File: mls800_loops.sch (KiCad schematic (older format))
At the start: 52 parts, among them J10 JACK_2P_STACK, J11 JACK_2P_SW, J2 JACK_2P_SW, J3 JACK_2P_STACK, J4 JACK_2P_STACK, J5 JACK_2P_STACK, J6 JACK_2P_STACK, J7 JACK_2P_STACK, J8 JACK_2P_STACK, J9 JACK_2P_STACK, Q1 2N3904, Q10 2N3904, Q11 2N3904, Q12 2N3904, Q13 2N3904, Q14 2N3904, Q15 2N3904, Q16 2N3904, Q2 2N3904, Q3 2N3904, Q4 2N3904, Q5 2N3904, Q6 2N3904, Q7 2N3904, Q8 2N3904, Q9 2N3904, U4 MCP23017

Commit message: MLS800
* unsplit AGND and DGND
* retouted relays
* relayout of gnd zone
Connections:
- net labels added: GND
- net labels removed: DGND
- wire segments 286 -> 289

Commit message: MLS800
* changed AGND to GND in jack connectors
* started front panel rerouting
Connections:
- net labels removed: AGND
- wire segments 289 -> 286
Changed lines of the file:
@@
 	0    1    1    0
 $EndComp
-$Comp
-L GND #PWR086
-U 1 1 54B7C949
-P 1600 3800
-F 0 "#PWR086" H 1600 3800 30  0001 C CNN
-F 1 "GND" H 1600 3730 30  0001 C CNN
-F 2 "" H 1600 3800 60  0000 C CNN
-F 3 "" H 1600 3800 60  0000 C CNN
-	1    1600 3800
-	1    0    0    -1
-$EndComp
-$Comp
-L AGND #PWR087
-U 1 1 54B7C999
-P 1750 3800
-F 0 "#PWR087" H 1750 3800 40  0001 C CNN
-F 1 "AGND" H 1750 3730 50  0000 C CNN
-F 2 "" H 1750 3800 60  0000 C CNN
-F 3 "" H 1750 3800 60  0000 C CNN
-	1    1750 3800
-	1    0    0    -1
-$EndComp
-Wire Wire Line
-	1600 3800 1600 3750
-Wire Wire Line
-	1600 3750 1750 3750
-Wire Wire Line
-	1750 3750 1750 3800
 $EndSCHEMATC

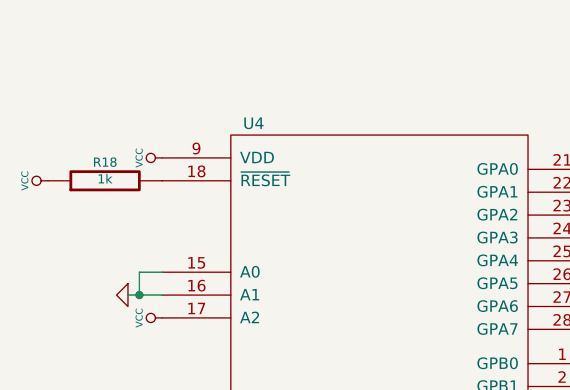
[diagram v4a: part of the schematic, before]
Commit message: MLS800
* rerouting of some part
* added filter cap to each digital part
* added board filter cap
* set 3d shapes for remaining parts (missing custom parts)
* added footprint for small pushbutton
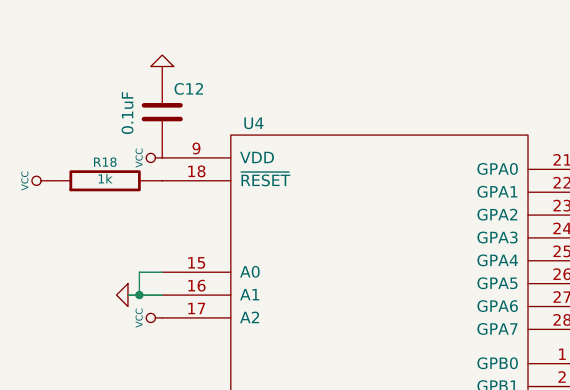
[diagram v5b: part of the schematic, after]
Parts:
- added C12: 0.1uF, Capacitors_SMD:C_0805_HandSoldering, symbol C
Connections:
- net GND: now also C12.1
- net VCC: now also C12.2

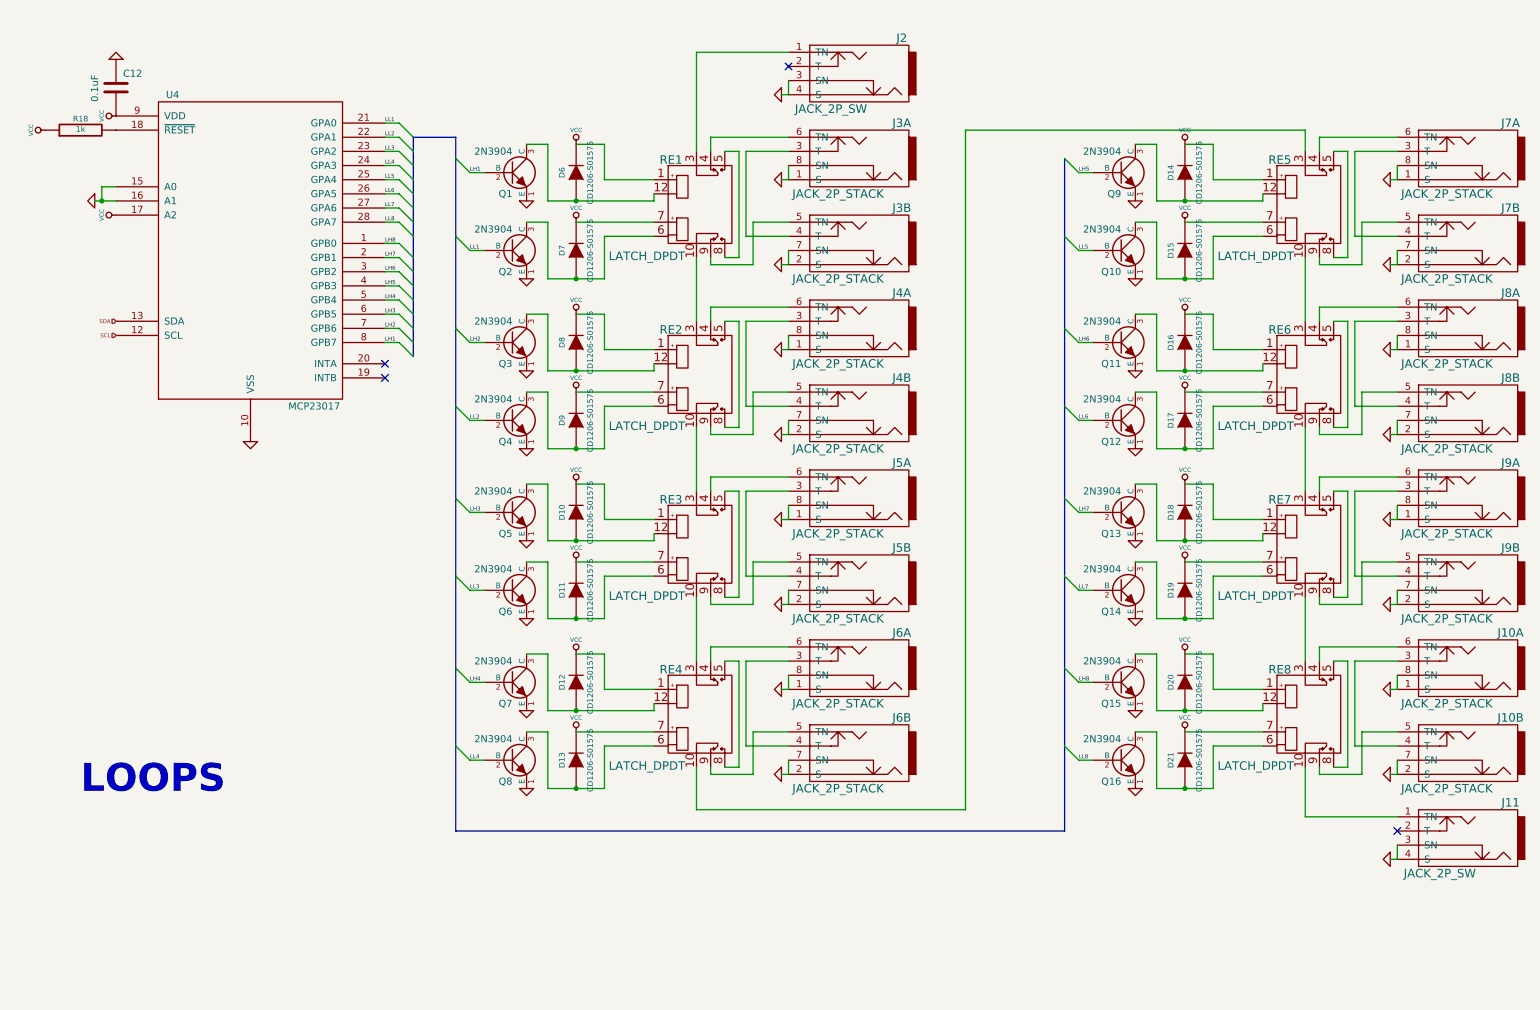
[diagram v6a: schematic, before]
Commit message: MLS800
* added ULN2803A
* relays schematics using 2 of the previous chip
* added an analog ground for jacks
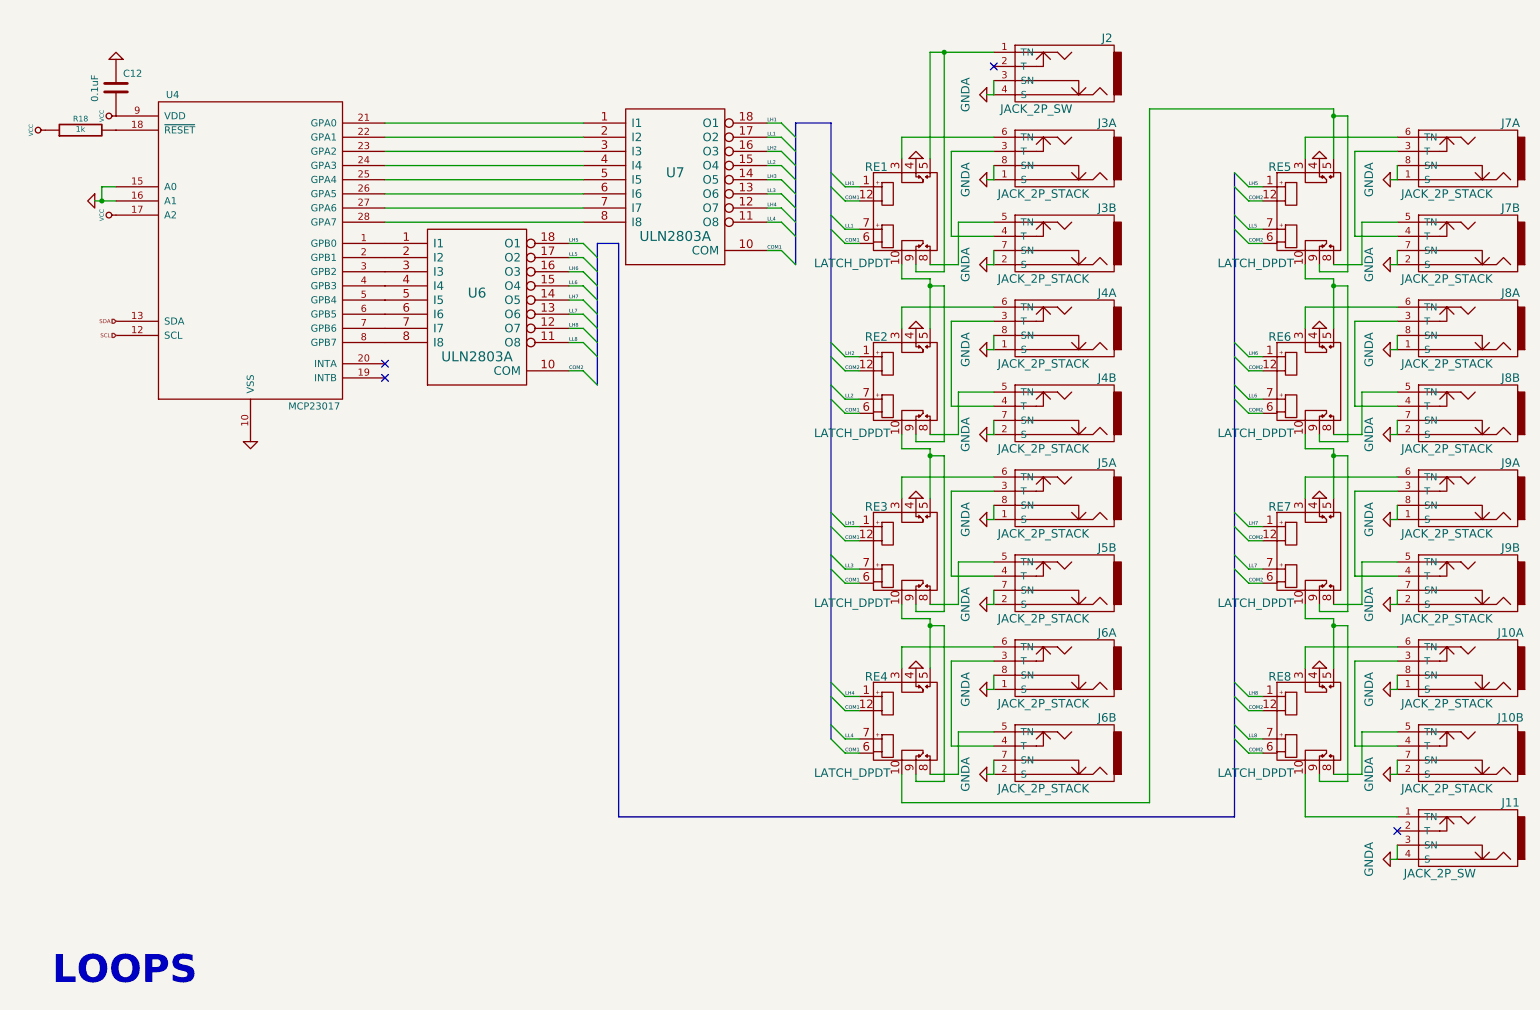
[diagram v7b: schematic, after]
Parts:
- removed D10, D11, D12, D13, D14, D15, D16, D17, D18, D19, D20, D21, D6, D7, D8, D9: CD1206-S01575, SMD_Packages:SMD-1206_Pol, symbol DIODE
- removed Q1, Q10, Q11, Q12, Q13, Q14, Q15, Q16, Q2, Q3, Q4, Q5, Q6, Q7, Q8, Q9: 2N3904, Housings_SOT-23_SOT-143_TSOT-6:SOT23_Transistor_Handsoldering_RevB_14Mar2014, symbol NPN
- added U6, U7: ULN2803A, Housings_SOIC:SOIC-18_7.5x11.6mm_Pitch1.27mm, symbol ULN2803A
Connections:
- net GND: now also RE1.4, RE2.4, RE3.4, RE4.4, RE5.4, RE6.4, RE7.4, RE8.4, U6.9 (GND), U7.9 (GND); no longer J10.1 (S), J10.2 (S), J10.7 (SN), J10.8 (SN), J11.3 (SN), J11.4 (S), J2.3 (SN), J2.4 (S), J3.1 (S), J3.2 (S), J3.7 (SN), J3.8 (SN), J4.1 (S), J4.2 (S), J4.7 (SN), J4.8 (SN), J5.1 (S), J5.2 (S), J5.7 (SN), J5.8 (SN), J6.1 (S), J6.2 (S), J6.7 (SN), J6.8 (SN), J7.1 (S), J7.2 (S), J7.7 (SN), J7.8 (SN), J8.1 (S), J8.2 (S), J8.7 (SN), J8.8 (SN), J9.1 (S), J9.2 (S), J9.7 (SN), J9.8 (SN)
- net LH1: now also RE1.1, U7.18 (O1); no longer U4.8 (GPB7)
- net LH2: now also RE2.1, U7.16 (O3); no longer U4.7 (GPB6)
- net LH3: now also RE3.1, U7.14 (O5); no longer U4.6 (GPB5)
- net LH4: now also RE4.1, U7.12 (O7); no longer U4.5 (GPB4)
- net LH5: now also RE5.1, U6.18 (O1); no longer U4.4 (GPB3)
- net LH6: now also RE6.1, U6.16 (O3); no longer U4.3 (GPB2)
- net LH7: now also RE7.1, U6.14 (O5); no longer U4.2 (GPB1)
- net LH8: now also RE8.1, U6.12 (O7); no longer U4.1 (GPB0)
- net LL1: now also RE1.7, U7.17 (O2); no longer U4.21 (GPA0)
- net LL2: now also RE2.7, U7.15 (O4); no longer U4.22 (GPA1)
- net LL3: now also RE3.7, U7.13 (O6); no longer U4.23 (GPA2)
- net LL4: now also RE4.7, U7.11 (O8); no longer U4.24 (GPA3)
- net LL5: now also RE5.7, U6.17 (O2); no longer U4.25 (GPA4)
- net LL6: now also RE6.7, U6.15 (O4); no longer U4.26 (GPA5)
- net LL7: now also RE7.7, U6.13 (O6); no longer U4.27 (GPA6)
- net LL8: now also RE8.7, U6.11 (O8); no longer U4.28 (GPA7)
- net VCC: no longer RE1.1, RE1.7, RE2.1, RE2.7, RE3.1, RE3.7, RE4.1, RE4.7, RE5.1, RE5.7, RE6.1, RE6.7, RE7.1, RE7.7, RE8.1, RE8.7
- net COM1: now reaches RE1.12
- net COM1: now also RE1.6, RE2.6, RE3.12, RE3.6, RE4.12, RE4.6, U7.10 (COM)
- net at RE1.10: now also RE2.5, RE2.9; no longer RE2.3
- net at RE1.3: now also J3.6 (TN); no longer J2.1 (TN)
- net at RE1.5: now also J2.1 (TN), RE1.9; no longer RE1.8
- net at J3.5 (TN): now also RE1.8; no longer RE1.9
- net COM2: now reaches RE2.12
- net COM2: now also RE5.12, RE5.6, RE6.12, RE6.6, RE7.12, RE7.6, RE8.12, RE8.6, U6.10 (COM)
- net at RE2.10: now also RE3.5, RE3.9; no longer RE3.3
- net at J4.6 (TN): now also RE2.3; no longer RE2.4
- net at RE2.8: now also J4.5 (TN); no longer RE2.5
- net at RE3.10: now also RE4.5, RE4.9; no longer RE4.3
- net at J5.6 (TN): now also RE3.3; no longer RE3.4
- net at RE3.8: now also J5.5 (TN); no longer RE3.5
- net at RE4.10: now also RE5.5, RE5.9; no longer RE5.3
- net at J6.6 (TN): now also RE4.3; no longer RE4.4
- net at RE4.8: now also J6.5 (TN); no longer RE4.5
- net at RE5.10: now also RE6.5, RE6.9; no longer RE6.3
- net at J7.6 (TN): now also RE5.3; no longer RE5.4
- net at RE5.8: now also J7.5 (TN); no longer RE5.5
- net at RE6.10: now also RE7.5, RE7.9; no longer RE7.3
- net at J8.6 (TN): now also RE6.3; no longer RE6.4
- net at RE6.8: now also J8.5 (TN); no longer RE6.5
- net at RE7.10: now also RE8.5, RE8.9; no longer RE8.3
- net at J9.6 (TN): now also RE7.3; no longer RE7.4
- net at RE7.8: now also J9.5 (TN); no longer RE7.5
- net at J10.6 (TN): now also RE8.3; no longer RE8.4
- net at RE8.8: now also J10.5 (TN); no longer RE8.5
- new net: U4.1 (GPB0), U6.1 (I1)
- new net: U4.2 (GPB1), U6.2 (I2)
- new net: U4.21 (GPA0), U7.1 (I1)
- new net: U4.22 (GPA1), U7.2 (I2)
- new net: U4.23 (GPA2), U7.3 (I3)
- new net: U4.24 (GPA3), U7.4 (I4)
- new net: U4.25 (GPA4), U7.5 (I5)
- new net: U4.26 (GPA5), U7.6 (I6)
- new net: U4.27 (GPA6), U7.7 (I7)
- new net: U4.28 (GPA7), U7.8 (I8)
- new net: U4.3 (GPB2), U6.3 (I3)
- new net: U4.4 (GPB3), U6.4 (I4)
- new net: U4.5 (GPB4), U6.5 (I5)
- new net: U4.6 (GPB5), U6.6 (I6)
- new net: U4.7 (GPB6), U6.7 (I7)
- new net: U4.8 (GPB7), U6.8 (I8)
- new net GNDA: J10.1 (S), J10.2 (S), J10.7 (SN), J10.8 (SN), J11.3 (SN), J11.4 (S), J2.3 (SN), J2.4 (S), J3.1 (S), J3.2 (S), J3.7 (SN), J3.8 (SN), J4.1 (S), J4.2 (S), J4.7 (SN), J4.8 (SN), J5.1 (S), J5.2 (S), J5.7 (SN), J5.8 (SN), J6.1 (S), J6.2 (S), J6.7 (SN), J6.8 (SN), J7.1 (S), J7.2 (S), J7.7 (SN), J7.8 (SN), J8.1 (S), J8.2 (S), J8.7 (SN), J8.8 (SN), J9.1 (S), J9.2 (S), J9.7 (SN), J9.8 (SN)
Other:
- moved on the sheet: J2, J3A, J3B, J4A, J4B, J5A, J5B, J6A, J6B, RE1, RE2, RE3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

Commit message: Added flyback diodes
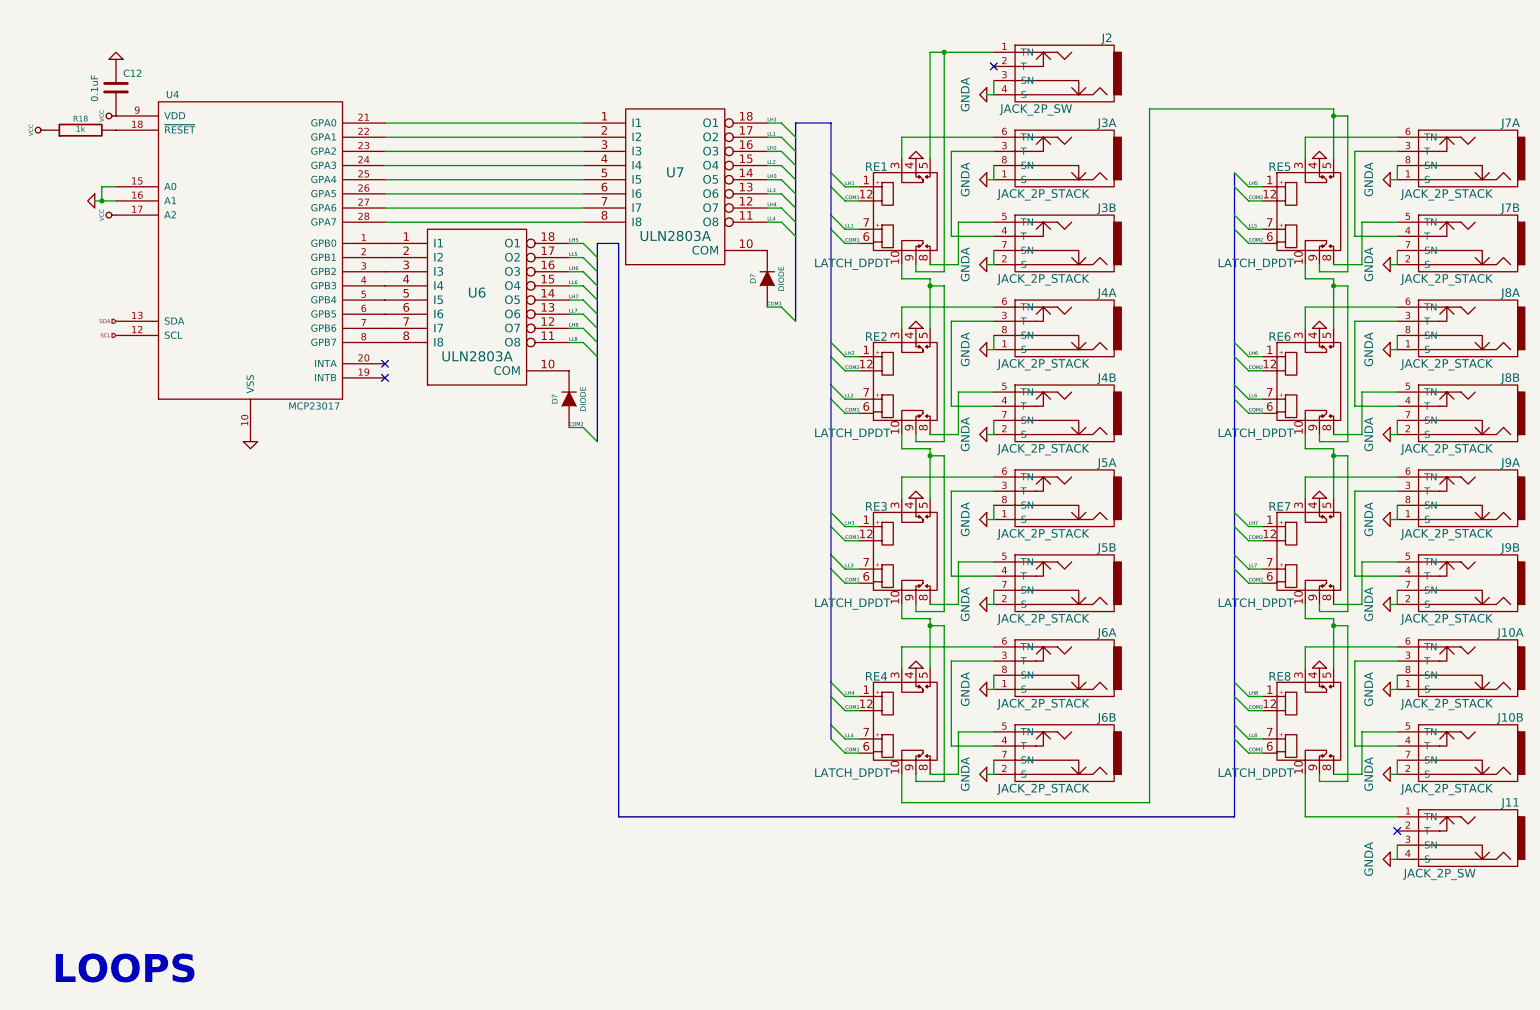
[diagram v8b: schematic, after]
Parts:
- added D? (x2): DIODE, SMD_Packages:SMD-1206_Pol, symbol DIODE
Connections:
- net COM1: now also D?.1 (A); no longer U7.10 (COM)
- net COM2: now also D?.1 (A); no longer U6.10 (COM)
- new net: D?.2 (K), U7.10 (COM)
- new net: D?.2 (K), U6.10 (COM)
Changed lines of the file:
@@
 	5800 1800 5900 1900
 Entry Wire Line
-	5800 2000 5900 2100
+	5800 2400 5900 2500
 Entry Wire Line
 	4400 1950 4500 2050
@@
 	4400 2650 4500 2750
 Entry Wire Line
-	4400 2850 4500 2950
+	4400 3250 4500 3350
 $Comp
 L GNDA #PWR046
@@
 	1100 1550 1000 1550
 Wire Wire Line
-	950  1650 1100 1650
+	950  1650 1000 1650
+Wire Wire Line
+	1000 1650 1100 1650
 Connection ~ 1000 1650
 Wire Wire Line
@@
 	4300 2650 4400 2650
 Wire Wire Line
-	4300 2850 4400 2850
-Wire Wire Line
 	5700 1100 5800 1100
 Wire Wire Line
@@
 	5700 1800 5800 1800
 Wire Wire Line
-	5700 2000 5800 2000
-Wire Wire Line
 	4400 1100 3000 1100
 Wire Wire Line
@@
 	6850 1350 6850 600
 Wire Wire Line
-	6850 600  7300 600
+	6850 600  6950 600
+Wire Wire Line
+	6950 600  7300 600
 Wire Wire Line
 	7050 2100 6850 2100
@@
 	7050 3300 6850 3300
 Wire Wire Line
-	6850 2550 6850 2200
+	6850 2200 6850 2250
+Wire Wire Line
+	6850 2250 6850 2550
 Wire Wire Line
 	6850 2200 6650 2200
@@
 	6650 3400 6850 3400
 Wire Wire Line
-	6850 3400 6850 3750
+	6850 3400 6850 3450
+Wire Wire Line
+	6850 3450 6850 3750
 Wire Wire Line
 	6850 3450 6950 3450
@@
 	6650 4600 6850 4600
 Wire Wire Line
-	6850 4600 6850 4950
+	6850 4600 6850 4650
+Wire Wire Line
+	6850 4650 6850 4950
 Wire Wire Line
 	7300 3600 6650 3600
@@
 	9800 2150 9800 1050
 Wire Wire Line
-	9700 1350 9700 1000
+	9700 1000 9700 1050
+Wire Wire Line
+	9700 1050 9700 1350
 Wire Wire Line
 	9800 1050 9700 1050
@@
 	9500 2200 9700 2200
 Wire Wire Line
-	9700 2200 9700 2550
+	9700 2200 9700 2250
+Wire Wire Line
+	9700 2250 9700 2550
 Wire Wire Line
 	10150 2400 9500 2400
@@
 	9500 3400 9700 3400
 Wire Wire Line
-	9700 3400 9700 3750
+	9700 3400 9700 3450
+Wire Wire Line
+	9700 3450 9700 3750
 Wire Wire Line
 	9600 4500 9600 4550
@@
 	9500 4600 9700 4600
 Wire Wire Line
-	9700 4600 9700 4950
+	9700 4600 9700 4650
+Wire Wire Line
+	9700 4650 9700 4950
 Wire Wire Line
 	9600 5700 9600 5750
@@
 	6350 5550 6250 5550
 Wire Bus Line
-	5900 2100 5900 1100
+	5900 1100 5900 1200
+Wire Bus Line
+	5900 1200 5900 1300
+Wire Bus Line
+	5900 1300 5900 1400
+Wire Bus Line
+	5900 1400 5900 1500
+Wire Bus Line
+	5900 1500 5900 1600
+Wire Bus Line
+	5900 1600 5900 1700
+Wire Bus Line
+	5900 1700 5900 1800
+Wire Bus Line
+	5900 1800 5900 1900
+Wire Bus Line
+	5900 1900 5900 2500
 Wire Bus Line
 	5900 1100 6150 1100
 Wire Bus Line
-	6150 1100 6150 5450
-Wire Bus Line
-	4500 2950 4500 1950
+	6150 1100 6150 1450
+Wire Bus Line
+	6150 1450 6150 1550
+Wire Bus Line
+	6150 1550 6150 1750
+Wire Bus Line
+	6150 1750 6150 1850
+Wire Bus Line
+	6150 1850 6150 2650
+Wire Bus Line
+	6150 2650 6150 2750
+Wire Bus Line
+	6150 2750 6150 2950
+Wire Bus Line
+	6150 2950 6150 3050
+Wire Bus Line
+	6150 3050 6150 3850
+Wire Bus Line
+	6150 3850 6150 3950
+Wire Bus Line
+	6150 3950 6150 4150
+Wire Bus Line
+	6150 4150 6150 4250
+Wire Bus Line
+	6150 4250 6150 5050
+Wire Bus Line
+	6150 5050 6150 5150
+Wire Bus Line
+	6150 5150 6150 5350
+Wire Bus Line
+	6150 5350 6150 5450
+Wire Bus Line
+	4500 1950 4500 2050
+Wire Bus Line
+	4500 2050 4500 2150
+Wire Bus Line
+	4500 2150 4500 2250
+Wire Bus Line
+	4500 2250 4500 2350
+Wire Bus Line
+	4500 2350 4500 2450
+Wire Bus Line
+	4500 2450 4500 2550
+Wire Bus Line
+	4500 2550 4500 2650
+Wire Bus Line
+	4500 2650 4500 2750
+Wire Bus Line
+	4500 2750 4500 3350
 Wire Bus Line
 	4500 1950 4650 1950
@@
 	4650 6000 9000 6000
 Wire Bus Line
-	9000 6000 9000 1450
-Text Label 5700 2000 0    25   ~ 0
+	9000 6000 9000 5450
+Wire Bus Line
+	9000 5450 9000 5350
+Wire Bus Line
+	9000 5350 9000 5150
+Wire Bus Line
+	9000 5150 9000 5050
+Wire Bus Line
+	9000 5050 9000 4250
+Wire Bus Line
+	9000 4250 9000 4150
+Wire Bus Line
+	9000 4150 9000 3950
+Wire Bus Line
+	9000 3950 9000 3850
+Wire Bus Line
+	9000 3850 9000 3050
+Wire Bus Line
+	9000 3050 9000 2950
+Wire Bus Line
+	9000 2950 9000 2750
+Wire Bus Line
+	9000 2750 9000 2650
+Wire Bus Line
+	9000 2650 9000 1850
+Wire Bus Line
+	9000 1850 9000 1750
+Wire Bus Line
+	9000 1750 9000 1550
+Wire Bus Line
+	9000 1550 9000 1450
+Text Label 5700 2400 0    25   ~ 0
 COM1
 Text Label 6250 1650 0    25   ~ 0
@@
 Text Label 9100 1850 0    25   ~ 0
 LL5
-Text Label 4300 2850 0    25   ~ 0
+Text Label 4300 3250 0    25   ~ 0
 COM2
 Text Label 5700 1100 0    25   ~ 0
@@
 Text Label 4300 2650 0    25   ~ 0
 LL8
+$Comp
+L DIODE D?
+U 1 1 54EBC78B
+P 4300 3050
+F 0 "D?" H 4300 3150 40  0000 C CNN
+F 1 "DIODE" H 4300 2950 40  0000 C CNN
+F 2 "SMD_Packages:SMD-1206_Pol" H 4300 3050 60  0001 C CNN
+F 3 "" H 4300 3050 60  0000 C CNN
+	1    4300 3050
+	0    -1   -1   0
+$EndComp
+$Comp
+L DIODE D?
+U 1 1 54EBCC5A
+P 5700 2200
+F 0 "D?" H 5700 2300 40  0000 C CNN
+F 1 "DIODE" H 5700 2100 40  0000 C CNN
+F 2 "SMD_Packages:SMD-1206_Pol" H 5700 2200 60  0001 C CNN
+F 3 "" H 5700 2200 60  0000 C CNN
+	1    5700 2200
+	0    -1   -1   0
+$EndComp
+Wire Wire Line
+	4300 3250 4400 3250
+Wire Wire Line
+	5700 2400 5800 2400
 $EndSCHEMATC
